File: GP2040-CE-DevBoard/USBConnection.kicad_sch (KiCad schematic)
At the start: 6 parts, among them J1 USB_C_Receptacle, U1 NCP1117-3.3_TO252

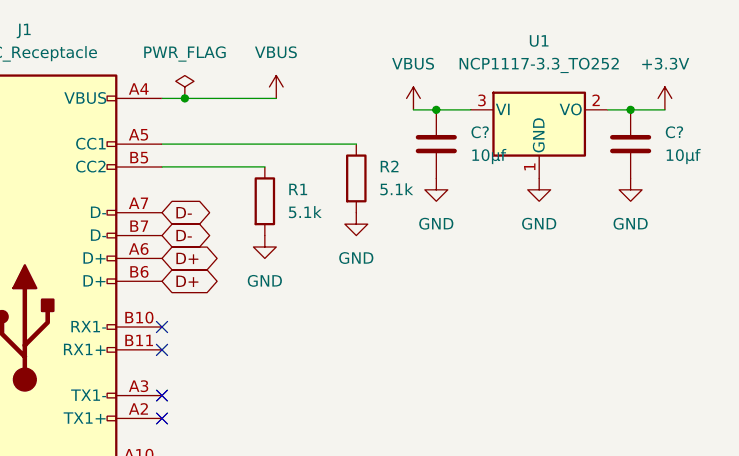
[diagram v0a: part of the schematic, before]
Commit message: Schematic nearly complete, PCB started
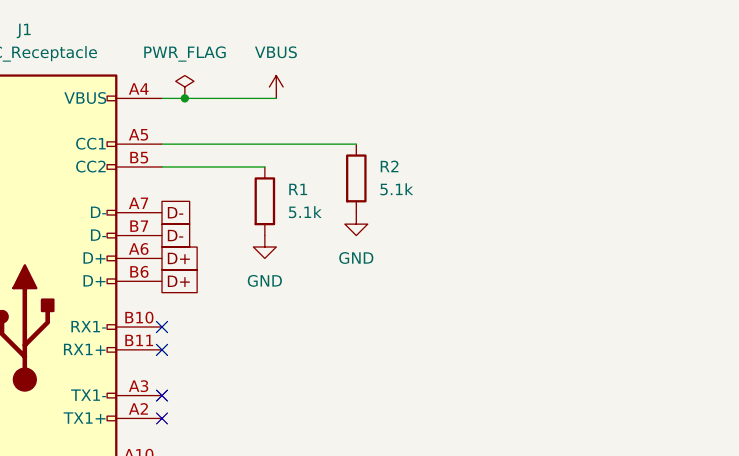
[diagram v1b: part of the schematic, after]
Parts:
- removed C? (x2): 10μf, Capacitor_SMD:C_0805_2012Metric_Pad1.18x1.45mm_HandSolder, symbol Device:C
- removed U1: NCP1117-3.3_TO252, Package_TO_SOT_SMD:TO-252-2, symbol Regulator_Linear:NCP1117-3.3_TO252
- J1: footprint (none) -> UJ31-CH-31-SMT-TR:CUI_UJ31-CH-31-SMT-TR
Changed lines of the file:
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@@
 (kicad_sch (version 20211123) (generator eeschema)
   (paper "A")
-  (junction (at 77.47 24.13) (diameter 0) (color 0 0 0 0)
-  )
   (junction (at 49.53 22.86) (diameter 0) (color 0 0 0 0)
-  )
-  (junction (at 99.06 24.13) (diameter 0) (color 0 0 0 0)
   )
   (no_connect (at 46.99 81.28))
@@
     (stroke (width 0) (type default) (color 0 0 0 0))
   )
-  (wire (pts (xy 77.47 24.13) (xy 81.28 24.13))
-    (stroke (width 0) (type default) (color 0 0 0 0))
-  )
-  (wire (pts (xy 99.06 24.13) (xy 96.52 24.13))
-    (stroke (width 0) (type default) (color 0 0 0 0))
-  )
   (wire (pts (xy 49.53 22.86) (xy 46.99 22.86))
     (stroke (width 0) (type default) (color 0 0 0 0))
   )
-  (wire (pts (xy 102.87 24.13) (xy 99.06 24.13))
-    (stroke (width 0) (type default) (color 0 0 0 0))
-  )
   (wire (pts (xy 46.99 27.94) (xy 68.58 27.94))
     (stroke (width 0) (type default) (color 0 0 0 0))
@@
     (stroke (width 0) (type default) (color 0 0 0 0))
   )
-  (wire (pts (xy 74.93 24.13) (xy 77.47 24.13))
-    (stroke (width 0) (type default) (color 0 0 0 0))
-  )
-  (global_label "D-" (shape bidirectional) (at 46.99 38.1 0) (fields_autoplaced)
+  (global_label "D-" (shape passive) (at 46.99 38.1 0) (fields_autoplaced)
     (effects (font (size 1.27 1.27)) (justify left))
     (property "Intersheet References" "${INTERSHEET_REFS}" (id 0) (at 52.2455 38.0206 0)
@@
     )
   )
-  (global_label "D-" (shape bidirectional) (at 46.99 35.56 0) (fields_autoplaced)
+  (global_label "D-" (shape passive) (at 46.99 35.56 0) (fields_autoplaced)
     (effects (font (size 1.27 1.27)) (justify left))
     (property "Intersheet References" "${INTERSHEET_REFS}" (id 0) (at 52.2455 35.4806 0)
@@
     )
   )
-  (global_label "D+" (shape bidirectional) (at 46.99 40.64 0) (fields_autoplaced)
+  (global_label "D+" (shape passive) (at 46.99 40.64 0) (fields_autoplaced)
     (effects (font (size 1.27 1.27)) (justify left))
     (property "Intersheet References" "${INTERSHEET_REFS}" (id 0) (at 52.2455 40.5606 0)
@@
     )
   )
-  (global_label "D+" (shape bidirectional) (at 46.99 43.18 0) (fields_autoplaced)
+  (global_label "D+" (shape passive) (at 46.99 43.18 0) (fields_autoplaced)
     (effects (font (size 1.27 1.27)) (justify left))
     (property "Intersheet References" "${INTERSHEET_REFS}" (id 0) (at 52.2455 43.1006 0)
       (effects (font (size 1.27 1.27)) (justify left) hide)
     )
-  )
-  (symbol (lib_id "Device:C") (at 77.47 27.94 0) (unit 1)
-    (in_bom yes) (on_board yes) (fields_autoplaced)
-    (property "Reference" "C?" (id 0) (at 81.28 26.6699 0)
-      (effects (font (size 1.27 1.27)) (justify left))
-    )
-    (property "Value" "10μf" (id 1) (at 81.28 29.2099 0)
-      (effects (font (size 1.27 1.27)) (justify left))
-    )
-    (property "Footprint" "Capacitor_SMD:C_0805_2012Metric_Pad1.18x1.45mm_HandSolder" (id 2) (at 78.4352 31.75 0)
-      (effects (font (size 1.27 1.27)) hide)
-    )
-    (property "Datasheet" "~" (id 3) (at 77.47 27.94 0)
-      (effects (font (size 1.27 1.27)) hide)
-    )
-    (pin "1")
-    (pin "2")
-  )
-  (symbol (lib_id "power:GND") (at 77.47 31.75 0) (unit 1)
-    (in_bom yes) (on_board yes) (fields_autoplaced)
-    (property "Reference" "#PWR?" (id 0) (at 77.47 38.1 0)
-      (effects (font (size 1.27 1.27)) hide)
-    )
-    (property "Value" "GND" (id 1) (at 77.47 36.83 0))
-    (property "Footprint" "" (id 2) (at 77.47 31.75 0)
-      (effects (font (size 1.27 1.27)) hide)
-    )
-    (property "Datasheet" "" (id 3) (at 77.47 31.75 0)
-      (effects (font (size 1.27 1.27)) hide)
-    )
-    (pin "1")
   )
   (symbol (lib_id "power:PWR_FLAG") (at 19.05 102.87 0) (unit 1)
@@
     (pin "1")
   )
-  (symbol (lib_id "power:GND") (at 99.06 31.75 0) (unit 1)
-    (in_bom yes) (on_board yes) (fields_autoplaced)
-    (property "Reference" "#PWR?" (id 0) (at 99.06 38.1 0)
-      (effects (font (size 1.27 1.27)) hide)
-    )
-    (property "Value" "GND" (id 1) (at 99.06 36.83 0))
-    (property "Footprint" "" (id 2) (at 99.06 31.75 0)
-      (effects (font (size 1.27 1.27)) hide)
-    )
-    (property "Datasheet" "" (id 3) (at 99.06 31.75 0)
-      (effects (font (size 1.27 1.27)) hide)
-    )
-    (pin "1")
-  )
-  (symbol (lib_id "power:+3.3V") (at 102.87 24.13 0) (unit 1)
-    (in_bom yes) (on_board yes) (fields_autoplaced)
-    (property "Reference" "#PWR09" (id 0) (at 102.87 27.94 0)
-      (effects (font (size 1.27 1.27)) hide)
-    )
-    (property "Value" "+3.3V" (id 1) (at 102.87 19.05 0))
-    (property "Footprint" "" (id 2) (at 102.87 24.13 0)
-      (effects (font (size 1.27 1.27)) hide)
-    )
-    (property "Datasheet" "" (id 3) (at 102.87 24.13 0)
-      (effects (font (size 1.27 1.27)) hide)
-    )
-    (pin "1")
-  )
-  (symbol (lib_id "Regulator_Linear:NCP1117-3.3_TO252") (at 88.9 24.13 0) (unit 1)
-    (in_bom yes) (on_board yes) (fields_autoplaced)
-    (property "Reference" "U1" (id 0) (at 88.9 16.51 0))
-    (property "Value" "NCP1117-3.3_TO252" (id 1) (at 88.9 19.05 0))
-    (property "Footprint" "Package_TO_SOT_SMD:TO-252-2" (id 2) (at 88.9 18.415 0)
-      (effects (font (size 1.27 1.27)) hide)
-    )
-    (property "Datasheet" "http://www.onsemi.com/pub_link/Collateral/NCP1117-D.PDF" (id 3) (at 88.9 24.13 0)
-      (effects (font (size 1.27 1.27)) hide)
-    )
-    (pin "1")
-    (pin "2")
-    (pin "3")
-  )
   (symbol (lib_id "power:GND") (at 19.05 102.87 0) (unit 1)
     (in_bom yes) (on_board yes) (fields_autoplaced)
@@
     (pin "1")
   )
-  (symbol (lib_id "power:GND") (at 88.9 31.75 0) (unit 1)
-    (in_bom yes) (on_board yes) (fields_autoplaced)
-    (property "Reference" "#PWR08" (id 0) (at 88.9 38.1 0)
-      (effects (font (size 1.27 1.27)) hide)
-    )
-    (property "Value" "GND" (id 1) (at 88.9 36.83 0))
-    (property "Footprint" "" (id 2) (at 88.9 31.75 0)
-      (effects (font (size 1.27 1.27)) hide)
-    )
-    (property "Datasheet" "" (id 3) (at 88.9 31.75 0)
-      (effects (font (size 1.27 1.27)) hide)
-    )
-    (pin "1")
-  )
   (symbol (lib_id "Connector:USB_C_Receptacle") (at 31.75 48.26 0) (unit 1)
     (in_bom yes) (on_board yes) (fields_autoplaced)
     (property "Reference" "J1" (id 0) (at 31.75 15.24 0))
     (property "Value" "USB_C_Receptacle" (id 1) (at 31.75 17.78 0))
-    (property "Footprint" "" (id 2) (at 35.56 48.26 0)
+    (property "Footprint" "UJ31-CH-31-SMT-TR:CUI_UJ31-CH-31-SMT-TR" (id 2) (at 35.56 48.26 0)
       (effects (font (size 1.27 1.27)) hide)
     )
@@
     (pin "2")
   )
-  (symbol (lib_id "Device:C") (at 99.06 27.94 0) (unit 1)
-    (in_bom yes) (on_board yes) (fields_autoplaced)
-    (property "Reference" "C?" (id 0) (at 102.87 26.6699 0)
-      (effects (font (size 1.27 1.27)) (justify left))
-    )
-    (property "Value" "10μf" (id 1) (at 102.87 29.2099 0)
-      (effects (font (size 1.27 1.27)) (justify left))
-    )
-    (property "Footprint" "Capacitor_SMD:C_0805_2012Metric_Pad1.18x1.45mm_HandSolder" (id 2) (at 100.0252 31.75 0)
-      (effects (font (size 1.27 1.27)) hide)
-    )
-    (property "Datasheet" "~" (id 3) (at 99.06 27.94 0)
-      (effects (font (size 1.27 1.27)) hide)
-    )
-    (pin "1")
-    (pin "2")
-  )
   (symbol (lib_id "power:GND") (at 68.58 35.56 0) (unit 1)
     (in_bom yes) (on_board yes) (fields_autoplaced)
@@
       (effects (font (size 1.27 1.27)) hide)
     )
-    (pin "1")
-  )
-  (symbol (lib_id "power:VBUS") (at 74.93 24.13 0) (unit 1)
-    (in_bom yes) (on_board yes) (fields_autoplaced)
-    (property "Reference" "#PWR07" (id 0) (at 74.93 27.94 0)
-      (effects (font (size 1.27 1.27)) hide)
-    )
-    (property "Value" "VBUS" (id 1) (at 74.93 19.05 0))
-    (property "Footprint" "" (id 2) (at 74.93 24.13 0)
-      (effects (font (size 1.27 1.27)) hide)
-    )
-    (property "Datasheet" "" (id 3) (at 74.93 24.13 0)
-      (effects (font (size 1.27 1.27)) hide)
-    )

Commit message: a lot of Silkscreen work
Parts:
- J1: footprint UJ31-CH-31-SMT-TR:CUI_UJ31-CH-31-SMT-TR -> Connector_USB:USB_C_Receptacle_GCT_USB4085
- R1, R2: footprint Resistor_SMD:R_0805_2012Metric_Pad1.20x1.40mm_HandSolder -> OpenStick:R_0805_2012Metric_Pad1.20x1.40mm_HandSolder
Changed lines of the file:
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@@
     (property "Reference" "J1" (id 0) (at 31.75 15.24 0))
     (property "Value" "USB_C_Receptacle" (id 1) (at 31.75 17.78 0))
-    (property "Footprint" "UJ31-CH-31-SMT-TR:CUI_UJ31-CH-31-SMT-TR" (id 2) (at 35.56 48.26 0)
+    (property "Footprint" "Connector_USB:USB_C_Receptacle_GCT_USB4085" (id 2) (at 35.56 48.26 0)
       (effects (font (size 1.27 1.27)) hide)
     )
@@
       (effects (font (size 1.27 1.27)) (justify left))
     )
-    (property "Footprint" "Resistor_SMD:R_0805_2012Metric_Pad1.20x1.40mm_HandSolder" (id 2) (at 56.642 34.29 90)
+    (property "Footprint" "OpenStick:R_0805_2012Metric_Pad1.20x1.40mm_HandSolder" (id 2) (at 56.642 34.29 90)
       (effects (font (size 1.27 1.27)) hide)
     )
@@
       (effects (font (size 1.27 1.27)) (justify left))
     )
-    (property "Footprint" "Resistor_SMD:R_0805_2012Metric_Pad1.20x1.40mm_HandSolder" (id 2) (at 66.802 31.75 90)
+    (property "Footprint" "OpenStick:R_0805_2012Metric_Pad1.20x1.40mm_HandSolder" (id 2) (at 66.802 31.75 90)
       (effects (font (size 1.27 1.27)) hide)
     )
